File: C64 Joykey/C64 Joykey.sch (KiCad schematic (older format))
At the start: 51 parts, among them J1 Port_1, J2 Port_2, M1 Mounting, M2 Mounting, M3 Mounting, M4 Mounting, Q1 2N3904, SW1 FIRE1, SW2 FIRE2, SW3 FIRE3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

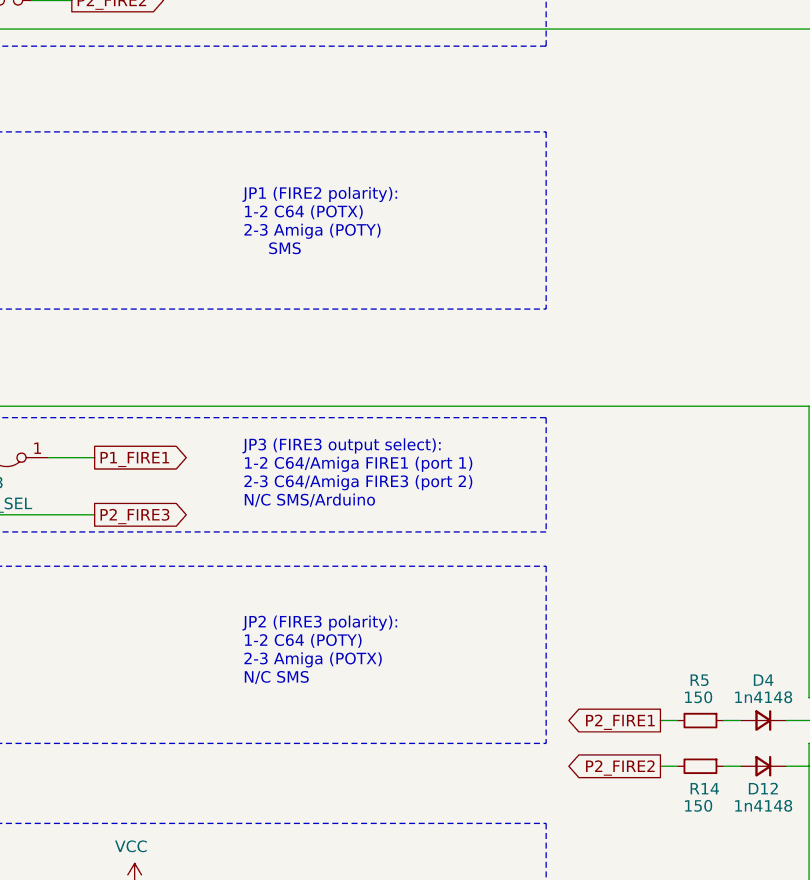
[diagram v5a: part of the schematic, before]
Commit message: Fixed Sinclair adapter
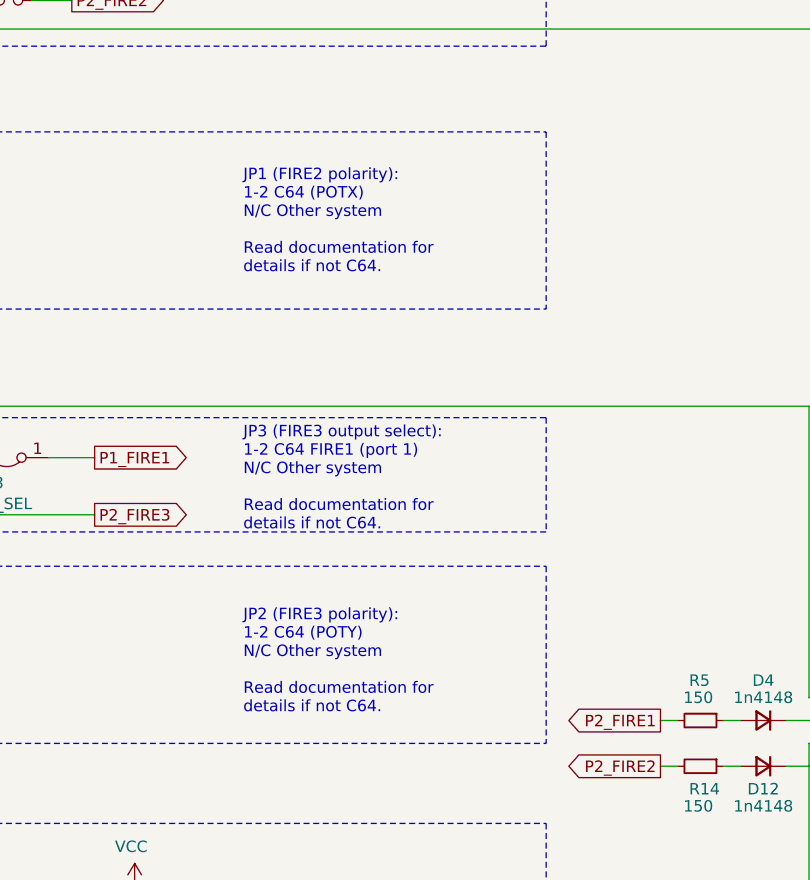
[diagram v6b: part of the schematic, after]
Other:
- note added: "JP1 (FIRE2 polarity):\n1-2 C64 (POTX)\nN/C Other system\n\nRead documentation for\ndetails if not C64."
- note added: "JP2 (FIRE3 polarity):\n1-2 C64 (POTY)\nN/C Other system\n\nRead documentation for\ndetails if not C64.\n"
- note added: "JP3 (FIRE3 output select):\n1-2 C64 FIRE1 (port 1)\nN/C Other system\n\nRead documentation for\ndetails if not C64."
- note removed: "JP1 (FIRE2 polarity):\n1-2 C64 (POTX)\n2-3 Amiga (POTY)\n SMS\n"
- note removed: "JP2 (FIRE3 polarity):\n1-2 C64 (POTY)\n2-3 Amiga (POTX)\nN/C SMS\n"
- note removed: "JP3 (FIRE3 output select):\n1-2 C64/Amiga FIRE1 (port 1)\n2-3 C64/Amiga FIRE3 (port 2)\nN/C SMS/Arduino"
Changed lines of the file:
@@
 	1    0    0    -1
 $EndComp
-Text Notes 4350 3275 0    50   ~ 0
-JP1 (FIRE2 polarity):\n1-2 C64 (POTX)\n2-3 Amiga (POTY)\n     SMS\n
-Text Notes 4350 5150 0    50   ~ 0
-JP2 (FIRE3 polarity):\n1-2 C64 (POTY)\n2-3 Amiga (POTX)\nN/C SMS\n
+Text Notes 4350 3350 0    50   ~ 0
+JP1 (FIRE2 polarity):\n1-2 C64 (POTX)\nN/C Other system\n\nRead documentation for\ndetails if not C64.
+Text Notes 4350 5275 0    50   ~ 0
+JP2 (FIRE3 polarity):\n1-2 C64 (POTY)\nN/C Other system\n\nRead documentation for\ndetails if not C64.\n
 Wire Wire Line
 	975  950  1200 950
@@
 Wire Wire Line
 	9025 5300 8875 5300
-Text Notes 4350 4375 0    50   ~ 0
-JP3 (FIRE3 output select):\n1-2 C64/Amiga FIRE1 (port 1)\n2-3 C64/Amiga FIRE3 (port 2)\nN/C SMS/Arduino
+Text Notes 4350 4475 0    50   ~ 0
+JP3 (FIRE3 output select):\n1-2 C64 FIRE1 (port 1)\nN/C Other system\n\nRead documentation for\ndetails if not C64.
 Wire Wire Line
 	6825 3925 6825 5200

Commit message: Added 10k resistors to isolate unpowered Arduino
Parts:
- removed D12: 1n4148, Diode_THT:D_DO-35_SOD27_P7.62mm_Horizontal, symbol Device:D_Small
- added R15, R16, R17, R18, R19, R20, R21: 10k, Resistor_THT:R_Axial_DIN0207_L6.3mm_D2.5mm_P10.16mm_Horizontal, symbol Device:R_Small
- J1: symbol c64_idc:C64_IDC2_OUT -> c64_idc:C64_IDC_PORT1
- J2: symbol c64_idc:C64_IDC2 -> c64_idc:C64_IDC_PORT2
- R14, R5: value 150 -> 10k
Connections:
- net FIRE1_IN: now also R17.1; no longer JP4.1, SW1.1
- net FIRE2_IN: now also R16.1; no longer JP6.1, SW2.1
- net FIRE2_OUT: now also R14.1
- net FIRE3_IN: now also R15.1; no longer JP3.2 (C), SW3.1
- net P2_DOWN: now also R20.1; no longer A1.16 (D15)
- net P2_LEFT: now also R21.1; no longer A1.15 (D14)
- net P2_RIGHT: now also R19.1; no longer A1.17 (D18)
- net P2_UP: now also R18.1; no longer A1.18 (D19)
- net VCC: now also J1.10 (EX_VCC), J2.10 (EX_VCC)
- new net: JP4.1, R17.2, SW1.1
- new net: JP6.1, R16.2, SW2.1
- new net: JP3.2 (C), R15.2, SW3.1
- new net: A1.15 (D14), R21.2
- new net: A1.16 (D15), R20.2
- new net: A1.17 (D18), R19.2
- new net: A1.18 (D19), R18.2
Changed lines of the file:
@@
 Title "C64 JoyKEY"
 Date ""
-Rev "C"
+Rev "D"
 Comp ""
 Comment1 ""
@@
 Wire Wire Line
 	2275 1350 2350 1350
-$Comp
-L c64_idc:C64_IDC2_OUT J1
-U 1 1 5FB76154
-P 8350 2200
-F 0 "J1" H 8400 2617 50  0000 C CNN
-F 1 "Port_1" H 8400 2526 50  0000 C CNN
-F 2 "C64 IDC:IDC_Joystick" H 8350 2200 50  0001 C CNN
-F 3 "~" H 8350 2200 50  0001 C CNN
-	1    8350 2200
-	1    0    0    -1
-$EndComp
 $Comp
 L power:GND #PWR03
@@
 Wire Wire Line
 	10325 1300 10325 1125
-Text GLabel 9025 5300 2    50   Input ~ 0
+Text GLabel 9300 5300 2    50   Input ~ 0
 P2_RIGHT
 Wire Wire Line
 	9025 5200 8875 5200
-Text GLabel 9025 5200 2    50   Input ~ 0
+Text GLabel 9300 5200 2    50   Input ~ 0
 P2_UP
 Wire Wire Line
 	9025 5500 8875 5500
-Text GLabel 9025 5400 2    50   Input ~ 0
+Text GLabel 9300 5400 2    50   Input ~ 0
 P2_DOWN
-Text GLabel 9025 5500 2    50   Input ~ 0
+Text GLabel 9300 5500 2    50   Input ~ 0
 P2_LEFT
 Wire Wire Line
@@
 JP3 (FIRE3 output select):\n1-2 C64 FIRE1 (port 1)\nN/C Other system\n\nRead documentation for\ndetails if not C64.
 Wire Wire Line
-	6825 3925 6825 5200
-Wire Wire Line
 	6825 5200 7925 5200
 Wire Wire Line
-	6925 2275 6925 5100
-Wire Wire Line
 	6925 5100 7925 5100
-Wire Wire Line
-	7025 1100 7025 5000
 Wire Wire Line
 	2550 1100 3025 1100
@@
 P 6350 5300
 F 0 "R5" V 6175 5250 50  0000 L CNN
-F 1 "150" V 6250 5225 50  0000 L CNN
+F 1 "10k" V 6250 5225 50  0000 L CNN
 F 2 "Resistor_THT:R_Axial_DIN0207_L6.3mm_D2.5mm_P10.16mm_Horizontal" H 6350 5300 50  0001 C CNN
 F 3 "~" H 6350 5300 50  0001 C CNN
@@
 	6175 5300 6250 5300
 $Comp
-L c64_idc:C64_IDC2 J2
+L c64_idc:C64_IDC_PORT2 J2
 U 1 1 5FB748C4
 P 8350 1400
@@
 P2_FIRE2
 $Comp
-L Device:D_Small D12
-U 1 1 600C6BE2
-P 6625 5500
-F 0 "D12" H 6625 5600 50  0000 C CNN
-F 1 "1n4148" H 6625 5675 50  0000 C CNN
-F 2 "Diode_THT:D_DO-35_SOD27_P7.62mm_Horizontal" V 6625 5500 50  0001 C CNN
-F 3 "~" V 6625 5500 50  0001 C CNN
-	1    6625 5500
-	-1   0    0    1
-$EndComp
-$Comp
 L Device:R_Small R14
 U 1 1 600C6BE8
 P 6350 5500
-F 0 "R14" V 6450 5450 50  0000 L CNN
-F 1 "150" V 6525 5425 50  0000 L CNN
+F 0 "R14" V 6450 5425 50  0000 L CNN
+F 1 "10k" V 6525 5425 50  0000 L CNN
 F 2 "Resistor_THT:R_Axial_DIN0207_L6.3mm_D2.5mm_P10.16mm_Horizontal" H 6350 5500 50  0001 C CNN
 F 3 "~" H 6350 5500 50  0001 C CNN
@@
 $EndComp
 Wire Wire Line
-	6450 5500 6525 5500
-Wire Wire Line
 	6175 5500 6250 5500
-Wire Wire Line
-	6725 5500 7925 5500
 Text Label 7900 5500 2    50   ~ 0
 FIRE2_OUT
@@
 Text Label 7900 5700 2    50   ~ 0
 PWR
-Wire Wire Line
-	7700 5700 7700 6425
-Wire Wire Line
-	7700 5700 7925 5700
-Wire Wire Line
-	7700 6425 10175 6425
 Text Label 7900 5400 2    50   ~ 0
 UNDERGLOW
@@
 Wire Wire Line
 	8400 4225 8400 4350
+$Comp
+L c64_idc:C64_IDC_PORT1 J1
+U 1 1 5FB76154
+P 8350 2200
+F 0 "J1" H 8400 2617 50  0000 C CNN
+F 1 "Port_1" H 8400 2526 50  0000 C CNN
+F 2 "C64 IDC:IDC_Joystick" H 8350 2200 50  0001 C CNN
+F 3 "~" H 8350 2200 50  0001 C CNN
+	1    8350 2200
+	1    0    0    -1
+$EndComp
+Wire Wire Line
+	8825 1600 10325 1600
+Wire Wire Line
+	10325 1600 10325 1300
+Connection ~ 10325 1300
+Wire Wire Line
+	10325 1600 10325 2400
+Wire Wire Line
+	10325 2400 8825 2400
+Connection ~ 10325 1600
+Wire Wire Line
+	7575 6425 7575 5700
+Wire Wire Line
+	7575 5700 7925 5700
+Wire Wire Line
+	7575 6425 10175 6425
+$Comp
+L Device:R_Small R18
+U 1 1 603170B6
+P 9125 5200
+F 0 "R18" V 9075 4950 50  0000 L CNN
+F 1 "10k" V 9125 5150 31  0000 L CNN
+F 2 "Resistor_THT:R_Axial_DIN0207_L6.3mm_D2.5mm_P10.16mm_Horizontal" H 9125 5200 50  0001 C CNN
+F 3 "~" H 9125 5200 50  0001 C CNN
+	1    9125 5200
+	0    1    1    0
+$EndComp
+Wire Wire Line
+	9225 5200 9300 5200
+$Comp
+L Device:R_Small R19
+U 1 1 6034215B
+P 9125 5300
+F 0 "R19" V 9075 5050 50  0000 L CNN
+F 1 "10k" V 9125 5250 31  0000 L CNN
+F 2 "Resistor_THT:R_Axial_DIN0207_L6.3mm_D2.5mm_P10.16mm_Horizontal" H 9125 5300 50  0001 C CNN
+F 3 "~" H 9125 5300 50  0001 C CNN
+	1    9125 5300
+	0    1    1    0
+$EndComp
+Wire Wire Line
+	9225 5300 9300 5300
+$Comp
+L Device:R_Small R20
+U 1 1 603493E3
+P 9125 5400
+F 0 "R20" V 9075 5150 50  0000 L CNN
+F 1 "10k" V 9125 5350 31  0000 L CNN
+F 2 "Resistor_THT:R_Axial_DIN0207_L6.3mm_D2.5mm_P10.16mm_Horizontal" H 9125 5400 50  0001 C CNN
+F 3 "~" H 9125 5400 50  0001 C CNN
+	1    9125 5400
+	0    1    1    0
+$EndComp
+Wire Wire Line
+	9225 5400 9300 5400
+$Comp
+L Device:R_Small R21
+U 1 1 60350811
+P 9125 5500
+F 0 "R21" V 9075 5250 50  0000 L CNN
+F 1 "10k" V 9125 5450 31  0000 L CNN
+F 2 "Resistor_THT:R_Axial_DIN0207_L6.3mm_D2.5mm_P10.16mm_Horizontal" H 9125 5500 50  0001 C CNN
+F 3 "~" H 9125 5500 50  0001 C CNN
+	1    9125 5500
+	0    1    1    0
+$EndComp
+Wire Wire Line
+	9225 5500 9300 5500
+$Comp
+L Device:R_Small R17
+U 1 1 60386764
+P 7025 4675
+F 0 "R17" V 7075 4425 50  0000 L CNN
+F 1 "10k" V 7025 4625 31  0000 L CNN
+F 2 "Resistor_THT:R_Axial_DIN0207_L6.3mm_D2.5mm_P10.16mm_Horizontal" H 7025 4675 50  0001 C CNN
+F 3 "~" H 7025 4675 50  0001 C CNN
+	1    7025 4675
+	-1   0    0    1
+$EndComp
+$Comp
+L Device:R_Small R16
+U 1 1 6038DB1E
+P 6925 4775
+F 0 "R16" V 6975 4525 50  0000 L CNN
+F 1 "10k" V 6925 4725 31  0000 L CNN
+F 2 "Resistor_THT:R_Axial_DIN0207_L6.3mm_D2.5mm_P10.16mm_Horizontal" H 6925 4775 50  0001 C CNN
+F 3 "~" H 6925 4775 50  0001 C CNN
+	1    6925 4775
+	-1   0    0    1
+$EndComp
+$Comp
+L Device:R_Small R15
+U 1 1 60394ED2
+P 6825 4875
+F 0 "R15" V 6875 4625 50  0000 L CNN
+F 1 "10k" V 6825 4825 31  0000 L CNN
+F 2 "Resistor_THT:R_Axial_DIN0207_L6.3mm_D2.5mm_P10.16mm_Horizontal" H 6825 4875 50  0001 C CNN
+F 3 "~" H 6825 4875 50  0001 C CNN
+	1    6825 4875
+	-1   0    0    1
+$EndComp
+Wire Wire Line
+	6825 4775 6825 3925
+Wire Wire Line
+	6925 4675 6925 2275
+Wire Wire Line
+	7025 4575 7025 1100
+Wire Wire Line
+	7025 4775 7025 5000
+Wire Wire Line
+	6925 4875 6925 5100
+Wire Wire Line
+	6825 4975 6825 5200
+Wire Wire Line
+	6450 5500 7925 5500
 $EndSCHEMATC

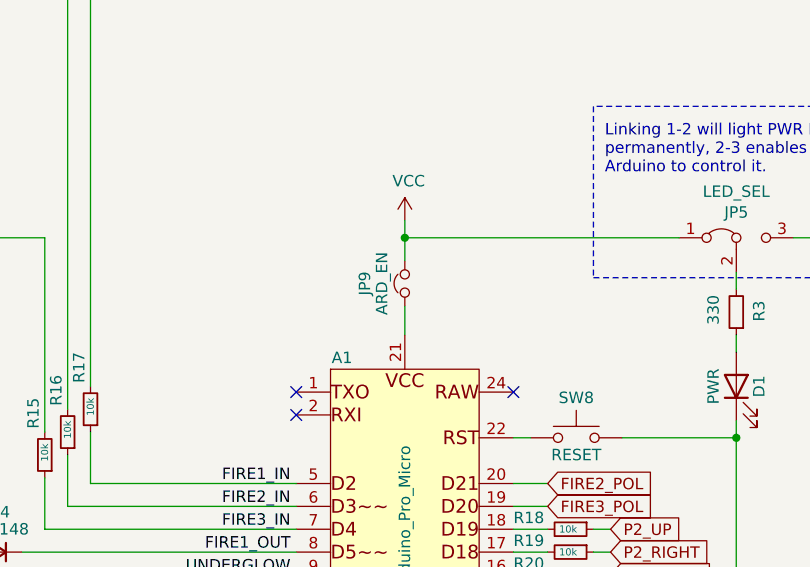
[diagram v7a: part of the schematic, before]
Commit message: New arcade layout
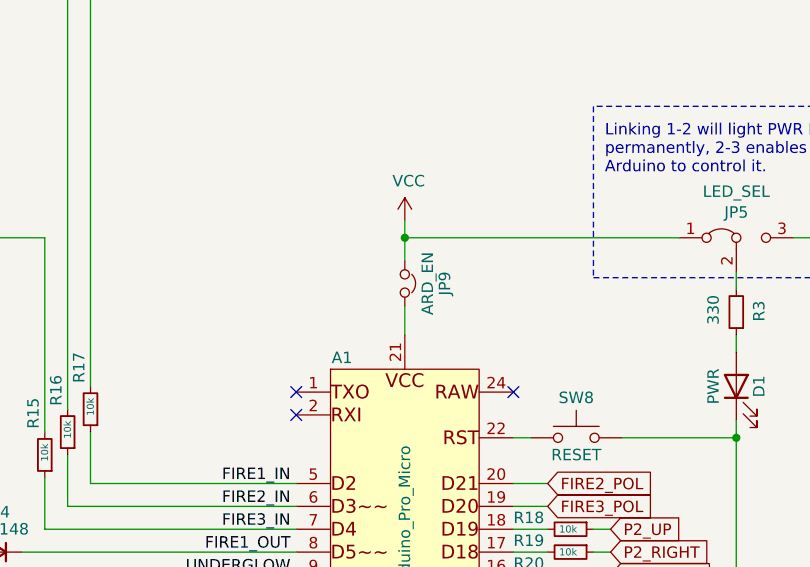
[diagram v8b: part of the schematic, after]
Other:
- moved on the sheet: JP9
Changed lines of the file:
@@
 F 3 "~" H 8400 4125 50  0001 C CNN
 	1    8400 4125
-	0    -1   -1   0
+	0    1    -1   0
 $EndComp
 Wire Wire Line
